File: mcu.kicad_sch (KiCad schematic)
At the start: 53 parts, among them J10 PinHeader_2x10_P1.27mm_SMD_Sh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, SW5 SW_B3U-1000P_SMD, SW6 CAS-120TA, U1 STM32H753ZIT6, Y1 Resonator_32.768kHz_ECX-31B, Y2 Oscillator_25MHz_ESC_2016MV

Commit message: [#95036] Add CAN bus subsheet
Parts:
- added R151: R_2k2_0402, antmicro-footprints:R_0402_1005Metric, symbol antmicroResistors0402:R_2k2_0402
- added R164: R_0R_0402, antmicro-footprints:R_0402_1005Metric, symbol antmicroResistors0402:R_0R_0402
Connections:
- net GPIO21: now also R164.1
- new net CAN_SHDN: R164.2
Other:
- note removed: "https://pinout.xyz/pinout/1_wire"

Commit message: [#95036] Add pullups to I2C
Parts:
- added R165, R167, R168, R170, R171, R173, R174: R_2k2_0402, antmicro-footprints:R_0402_1005Metric, symbol antmicroResistors0402:R_2k2_0402
- added R166, R169, R172: R_10k_0402, antmicro-footprints:R_0402_1005Metric, symbol antmicroResistors0402:R_10k_0402
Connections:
- net +3V3: now also R151.2, R165.1, R166.1, R167.2, R168.1, R169.1, R170.2, R171.1, R172.1, R173.2, R174.1
- net I2C1.SCL: now also R165.2
- net I2C1.SDA: now also R151.1
- net I2C2.SCL: now also R168.2
- net I2C2.SDA: now also R167.1
- net I2C3.SCL: now also R173.1
- net I2C3.SDA: now also R174.2
- net I2C4.SCL: now also R171.2
- net I2C4.SDA: now also R170.1
- net I2C1.INT renamed I2C1.~{INT}
- net I2C1.~{INT}: now also R166.2
- new net I2C2.~{INT}: R169.2
- new net I2C4.~{INT}: R172.2
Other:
- moved on the sheet: R151

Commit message: [#95036] Rearrange MCU scheet
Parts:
- removed R172: R_10k_0402, antmicro-footprints:R_0402_1005Metric, symbol antmicroResistors0402:R_10k_0402
- added D22: RB521S30T1G, antmicro-footprints:SOD-523, symbol antmicroDiodesRectifiersSingle:RB521S30T1G
- added R175: R_2k2_0402, antmicro-footprints:R_0402_1005Metric, symbol antmicroResistors0402:R_2k2_0402
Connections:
- net JTAG.RST is gone; now on net JTAG.~{RST}: J10.10
- net +3V3: now also D22.2 (A)
- net GND: now also BT1.2 (-), J10.11, J10.13, J10.9
- net MCU_VBAT: now also D22.1 (C), R175.2
- net MCU_VDDA: now also J10.1
- net at BT1.1 (+): now also R175.1
- net SPI_2.MISO renamed SPI_2.MISO_IO1
- net SPI_2.MOSI renamed SPI_2.MOSI_IO0
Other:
- note added: "STM32H753 MCU"
- note removed: "TODO: Verify all UARTs RX/TX cross. Should I make one?"
- moved on the sheet: BT1, C14, C15, C16, C17, C18, C19, C20, C21, C22, C23, C24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

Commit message: [#95036] Adjust MCU LSE clock
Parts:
- removed C22, C23: C_6p_0402, antmicro-footprints:C_0402_1005Metric, symbol antmicroCapacitors0402:C_6p_0402
- removed R16: R_1M_0402, antmicro-footprints:R_0402_1005Metric, symbol antmicroResistors0402:R_1M_0402
- added C22, C23: C_18p_0402, antmicro-footprints:C_0402_1005Metric, symbol antmicroCapacitors0402:C_18p_0402
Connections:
- net GND: now also C22.1, C23.1
- net at U1.8 (PC14-OSC32_IN), Y1.1: now also C22.2
- net at R15.1, Y1.2: now also C23.2
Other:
- note added: "CL=12.5pF CS~=3.5pF CL1=CL2=2(CL-CS)=18pF"
- note removed: "TODO Calculate oscilator capacitors"
- moved on the sheet: Y1

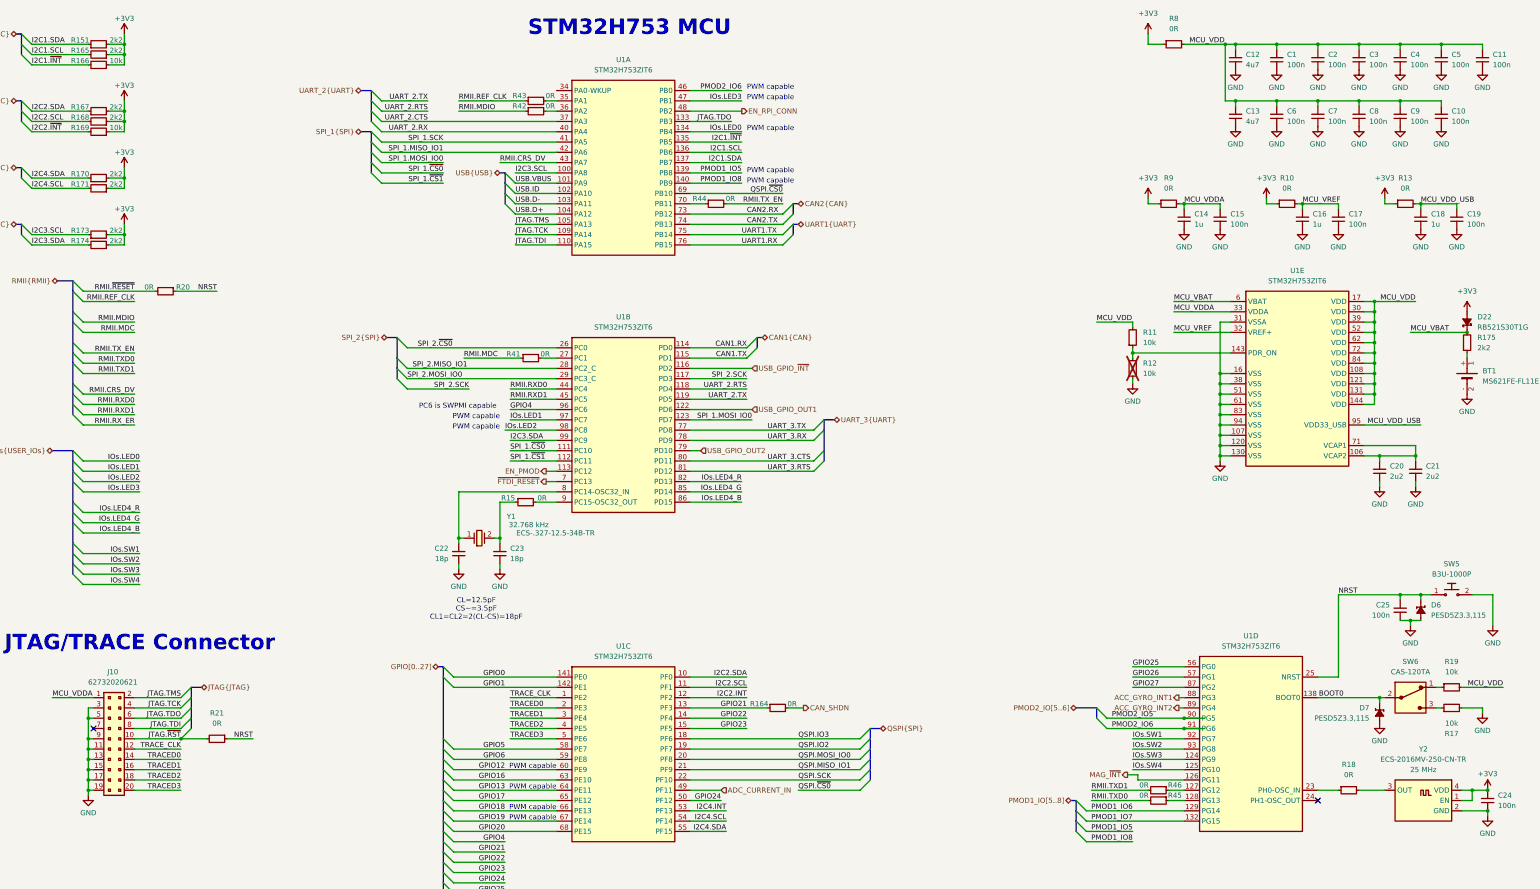
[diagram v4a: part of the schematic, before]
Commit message: [#95036] Solve basic ERCs
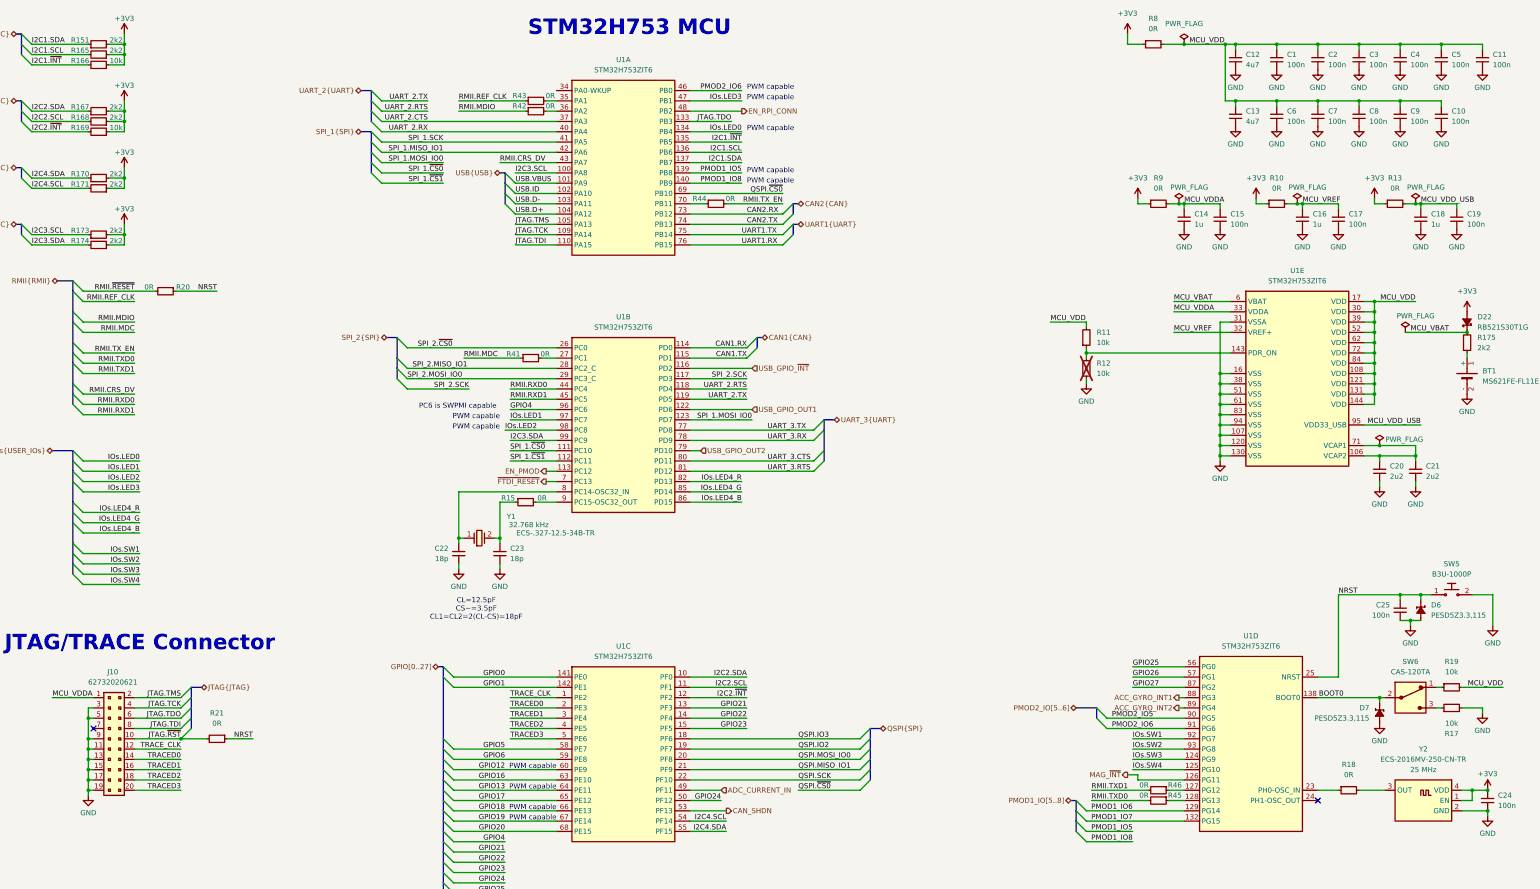
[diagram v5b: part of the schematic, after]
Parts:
- removed R164: R_0R_0402, antmicro-footprints:R_0402_1005Metric, symbol antmicroResistors0402:R_0R_0402
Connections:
- net I2C2.INT is gone; now on net I2C2.~{INT}: U1.12 (PF2)
- net I2C4.INT is gone; now on net CAN_SHDN: U1.53 (PF13)
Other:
- moved on the sheet: R10, R11, R12, R13, R8, R9

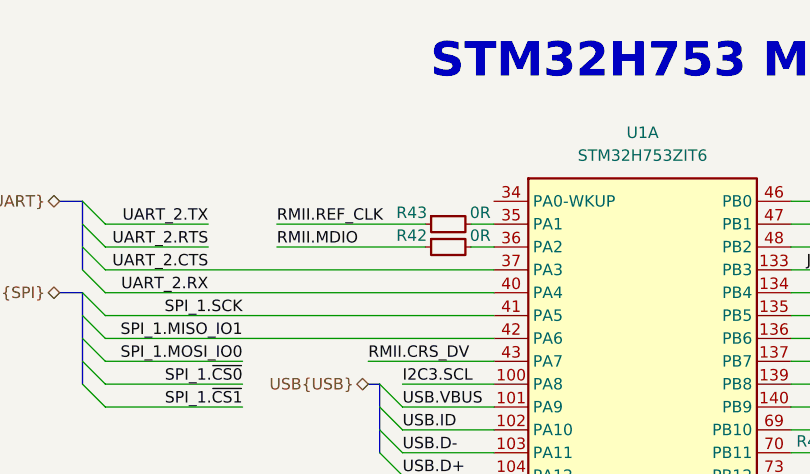
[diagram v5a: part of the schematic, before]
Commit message: [#95036] Replace barometer IC
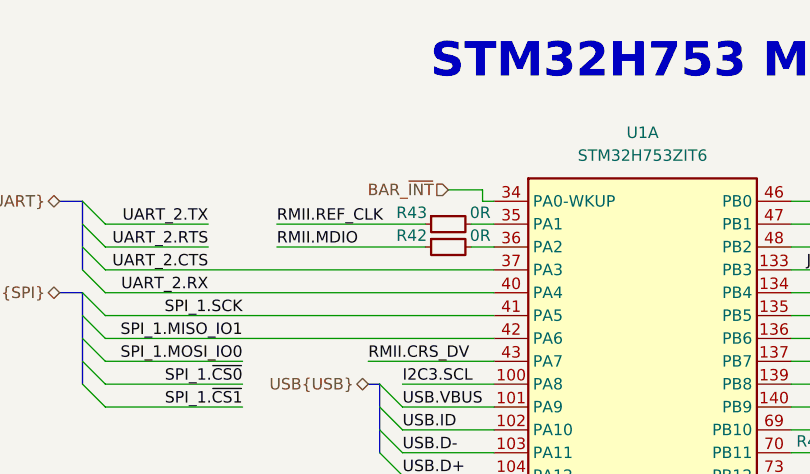
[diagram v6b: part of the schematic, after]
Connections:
- net BAR_~{INT}: now reaches U1.34 (PA0-WKUP)
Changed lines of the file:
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@@
 	(wire
 		(pts
+			(xy 161.29 39.37) (xy 162.56 39.37)
+		)
+		(stroke
+			(width 0)
+			(type default)
+		)
+	)
+	(wire
+		(pts
 			(xy 293.37 104.14) (xy 293.37 105.41)
 		)
@@
 	(wire
 		(pts
+			(xy 157.48 38.1) (xy 161.29 38.1)
+		)
+		(stroke
+			(width 0)
+			(type default)
+		)
+	)
+	(wire
+		(pts
 			(xy 365.76 189.23) (xy 365.76 190.5)
 		)
@@
 	(wire
 		(pts
+			(xy 161.29 38.1) (xy 161.29 39.37)
+		)
+		(stroke
+			(width 0)
+			(type default)
+		)
+	)
+	(wire
+		(pts
 			(xy 195.58 62.23) (xy 208.28 62.23)
 		)
@@
 		(effects
 			(font
+				(size 1.27 1.27)
+			)
+			(justify right)
+		)
+	)
+	(hierarchical_label "BAR_~{INT}"
+		(shape input)
+		(at 157.48 38.1 180)
+		(effects
+			(font

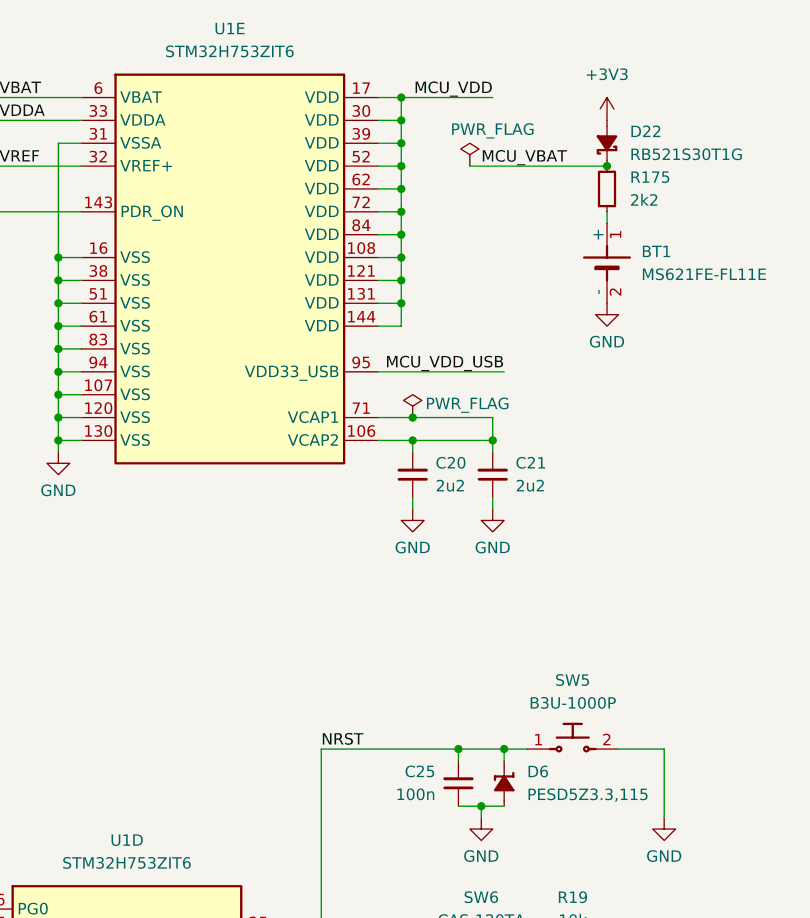
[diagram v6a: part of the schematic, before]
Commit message: [#95036] Add testpoints
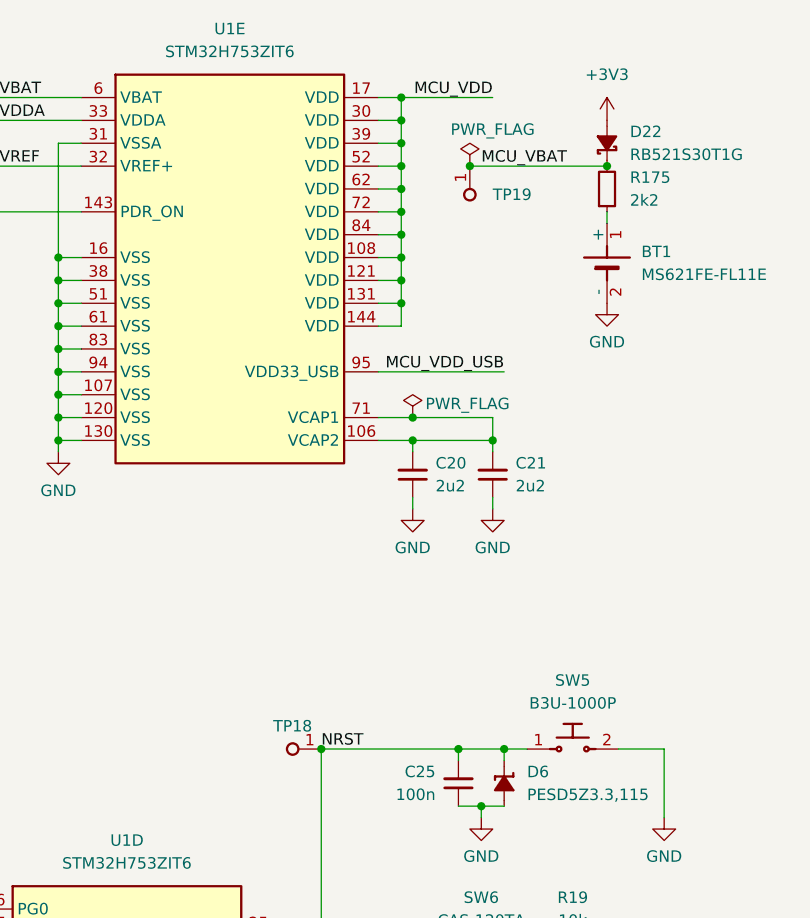
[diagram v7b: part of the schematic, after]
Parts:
- added TP18, TP19: TP_1mm_SMD, antmicro-footprints:TP_SMD_1mm, symbol antmicroTestPoints:TP_1mm_SMD
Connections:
- net MCU_VBAT: now also TP19.1
- net NRST: now also TP18.1
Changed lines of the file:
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@@
 	)
 	(junction
+		(at 355.6 163.83)
+		(diameter 0)
+		(color 0 0 0 0)
+	)
+	(junction
 		(at 381 27.94)
 		(diameter 0)
@@
 	)
 	(junction
+		(at 372.11 99.06)
+		(diameter 0)
+		(color 0 0 0 0)
+	)
+	(junction
 		(at 69.85 199.39)
 		(diameter 0)
@@
 	)
 	(symbol
+		(lib_id "antmicroTestPoints:TP_1mm_SMD")
+		(at 372.11 99.06 270)
+		(unit 1)
+		(exclude_from_sim no)
+		(in_bom no)
+		(on_board yes)
+		(dnp no)
+		(fields_autoplaced yes)
+		(property "Reference" "TP19"
+			(at 374.65 102.235 90)
+			(effects
+				(font
+					(size 1.27 1.27)
+					(thickness 0.15)
+				)
+				(justify left)
+			)
+		)
+		(property "Value" "TP_1mm_SMD"
+			(at 364.49 114.3 0)
+			(effects
+				(font
+					(size 1.27 1.27)
+					(thickness 0.15)
+				)
+				(justify left bottom)
+				(hide yes)
+			)
+		)
+		(property "Footprint" "antmicro-footprints:TP_SMD_1mm"
+			(at 361.95 114.3 0)
+			(effects
+				(font
+					(size 1.27 1.27)
+					(thickness 0.15)
+				)
+				(justify left bottom)
+				(hide yes)
+			)
+		)
+		(property "Datasheet" ""
+			(at 359.41 116.84 0)
+			(effects
+				(font
+					(size 1.27 1.27)
+					(thickness 0.15)
+				)
+				(justify left bottom)
+				(hide yes)
+			)
+		)
+		(property "Description" "Test point 1mm SMD"
+			(at 351.79 114.3 0)
+			(effects
+				(font
+					(size 1.27 1.27)
+				)
+				(justify left bottom)
+				(hide yes)
+			)
+		)
+		(property "MPN" ""
+			(at 372.11 99.06 0)
+			(effects
+				(font
+					(size 1.27 1.27)
+				)
+				(hide yes)
+			)
+		)
+		(property "Manufacturer" ""
+			(at 372.11 99.06 0)
+			(effects
+				(font
+					(size 1.27 1.27)
+				)
+				(hide yes)
+			)
+		)
+		(property "Author" "Antmicro"
+			(at 356.87 114.3 0)
+			(effects
+				(font
+					(size 1.27 1.27)
+					(thickness 0.15)
+				)
+				(justify left bottom)
+				(hide yes)
+			)
+		)
+		(property "License" "Apache-2.0"
+			(at 354.33 114.3 0)
+			(effects
+				(font
+					(size 1.27 1.27)
+					(thickness 0.15)
+				)
+				(justify left bottom)
+				(hide yes)
+			)
+		)
+		(pin "1"
+		)
+		(instances
+			(project "renode-reference-platform"
+				(path "/126ae87b-f292-4372-94ff-ae46971d67ab/a09bd19e-75b4-4cc2-9c76-c57ffa8ef2d8"
+					(reference "TP19")
+					(unit 1)
+				)
+			)
+		)
+	)
+	(symbol
 		(lib_id "antmicroCapacitors0402:C_1u_0402")
 		(at 317.5 73.66 90)
@@
 					(unit 1)
 				)
+			)
+		)
+	)
+	(symbol
+		(lib_id "antmicroTestPoints:TP_1mm_SMD")
+		(at 355.6 163.83 180)
+		(unit 1)
+		(exclude_from_sim no)
+		(in_bom no)
+		(on_board yes)
+		(dnp no)
+		(fields_autoplaced yes)
+		(property "Reference" "TP18"
+			(at 352.425 161.29 0)
+			(effects
+				(font
+					(size 1.27 1.27)
+					(thickness 0.15)
+				)
+			)
+		)
+		(property "Value" "TP_1mm_SMD"
+			(at 340.36 156.21 0)
+			(effects
+				(font
+					(size 1.27 1.27)
+					(thickness 0.15)
+				)
+				(justify left bottom)
+				(hide yes)
+			)
+		)
+		(property "Footprint" "antmicro-footprints:TP_SMD_1mm"
+			(at 340.36 153.67 0)
+			(effects
+				(font
+					(size 1.27 1.27)
+					(thickness 0.15)
+				)
+				(justify left bottom)
+				(hide yes)
+			)
+		)
+		(property "Datasheet" ""
+			(at 337.82 151.13 0)
+			(effects
+				(font
+					(size 1.27 1.27)
+					(thickness 0.15)
+				)
+				(justify left bottom)
+				(hide yes)
+			)
+		)
+		(property "Description" "Test point 1mm SMD"
+			(at 340.36 143.51 0)
+			(effects
+				(font
+					(size 1.27 1.27)
+				)
+				(justify left bottom)
+				(hide yes)
+			)
+		)
+		(property "MPN" ""
+			(at 355.6 163.83 0)
+			(effects
+				(font
+					(size 1.27 1.27)
+				)
+				(hide yes)
+			)
+		)
+		(property "Manufacturer" ""
+			(at 355.6 163.83 0)
+			(effects
+				(font
+					(size 1.27 1.27)
+				)
+				(hide yes)
+			)
+		)
+		(property "Author" "Antmicro"
+			(at 340.36 148.59 0)
+			(effects
+				(font
+					(size 1.27 1.27)
+					(thickness 0.15)
+				)
+				(justify left bottom)
+				(hide yes)
+			)
+		)
+		(property "License" "Apache-2.0"
+			(at 340.36 146.05 0)
+			(effects
+				(font
+					(size 1.27 1.27)
+					(thickness 0.15)
+				)
+				(justify left bottom)
+				(hide yes)
+			)
+		)
+		(pin "1"
+		)
+		(instances
+			(project "renode-reference-platform"
+				(path "/126ae87b-f292-4372-94ff-ae46971d67ab/a09bd19e-75b4-4cc2-9c76-c57ffa8ef2d8"
+					(reference "TP18")
+					(unit 1)
+				)
